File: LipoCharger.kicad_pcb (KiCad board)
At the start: 4 copper layers, 36.2 x 36 mm, 35 parts, among them J1 S2B-XH-A, J2 USB_C_Receptacle_USB2.0_14P, Q1 SI2300A, Q2 SI2300A, Q3 HL 2305A, SW1 SK12D07VG4, U1 TP4056-42-ESOP8, U2 MT3608, U3 FM2113

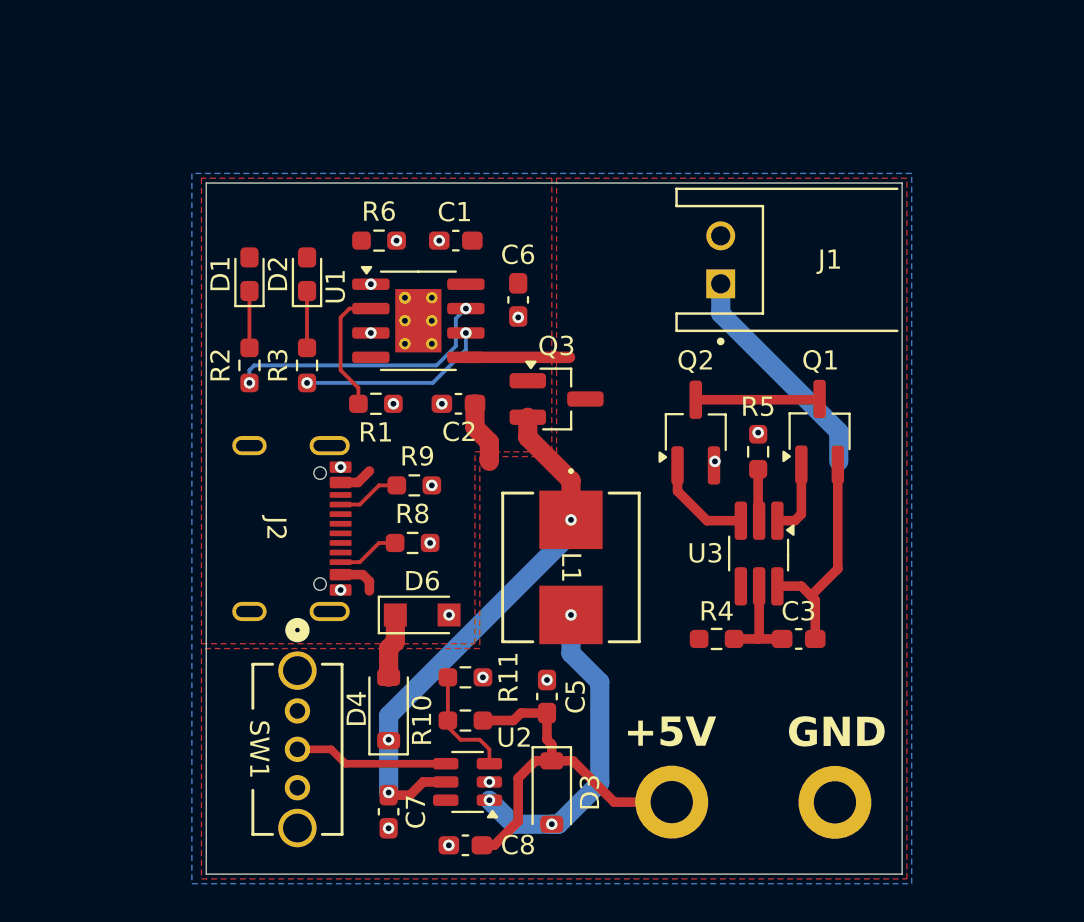
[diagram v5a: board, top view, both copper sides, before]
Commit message: Fixed most of the DRC
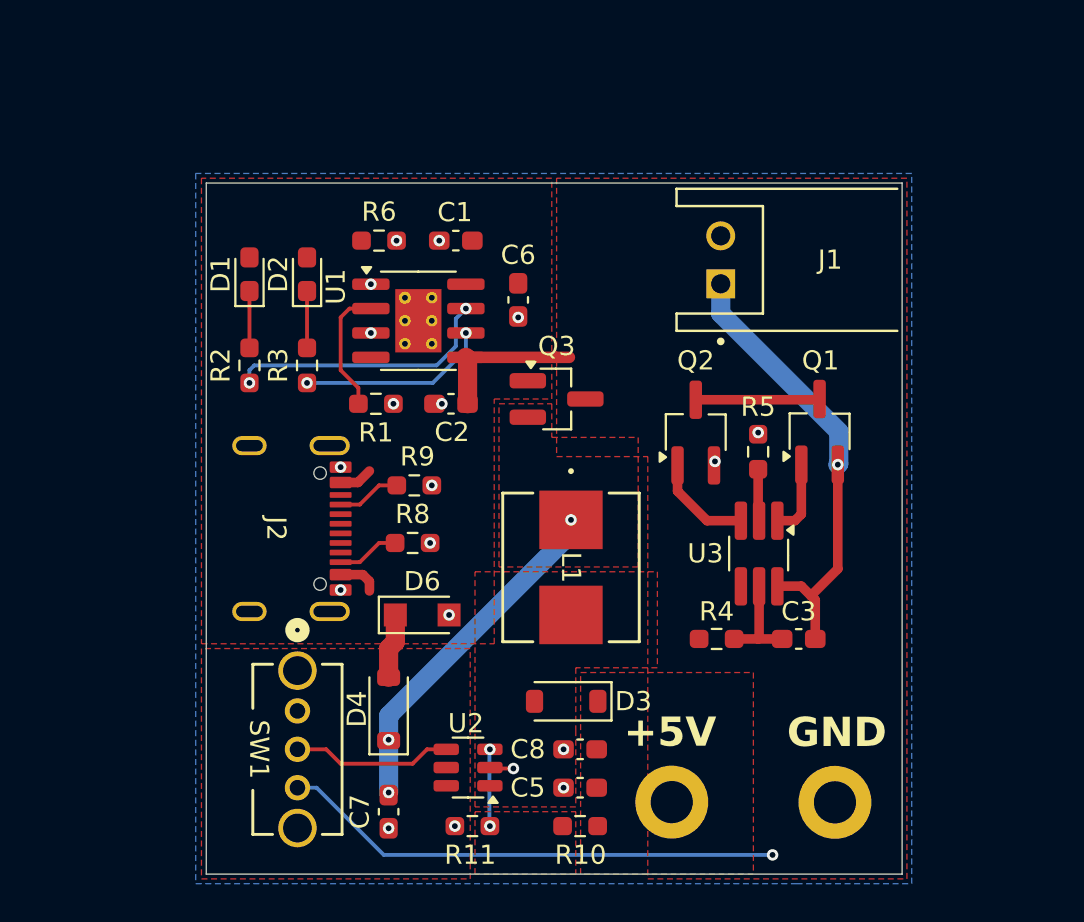
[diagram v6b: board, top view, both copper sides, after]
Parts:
- moved R10 8.12 mm to (49.7, 58.0)
- moved C8 7.79 mm to (49.7, 54.0)
- moved R11 7.76 mm to (44.1, 58.0), turned to 180 degrees
- moved C5 5.05 mm to (49.7, 56.0), turned to 180 degrees
- moved D3 4.81 mm to (49.0, 51.5), turned to 180 degrees
- moved U2 0.75 mm to (43.9, 55.0)
- moved C2 0.39 mm to (43.0, 36.0)
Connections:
- net Net-(D3-A) renamed /SW
- net Net-(D4-K) renamed BOOST_IN
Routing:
- net +BATT: track 8.82 -> 34.2 mm, vias 0 -> 1
- net Net-(D3-K): track 20.0 -> 0.00 mm
- net /SW: track 16.5 -> 0.00 mm, vias 3 -> 0
- net BOOST_IN: track 27.7 -> 18.1 mm
- net Net-(U2-FB): track 5.98 -> 4.02 mm, vias 0 -> 2
- net GND: track 0.31 -> 1.42 mm
- net -BATT: track 23.5 -> 23.7 mm, vias 0 -> 1
- added copper zone on F.Cu, net /SW
- added copper zone on F.Cu, net BOOST_IN
- added copper zone on F.Cu, net Net-(D3-K)
- added copper zone on F.Cu, net Net-(U2-FB)

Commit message: Moved vias outside off of the pads
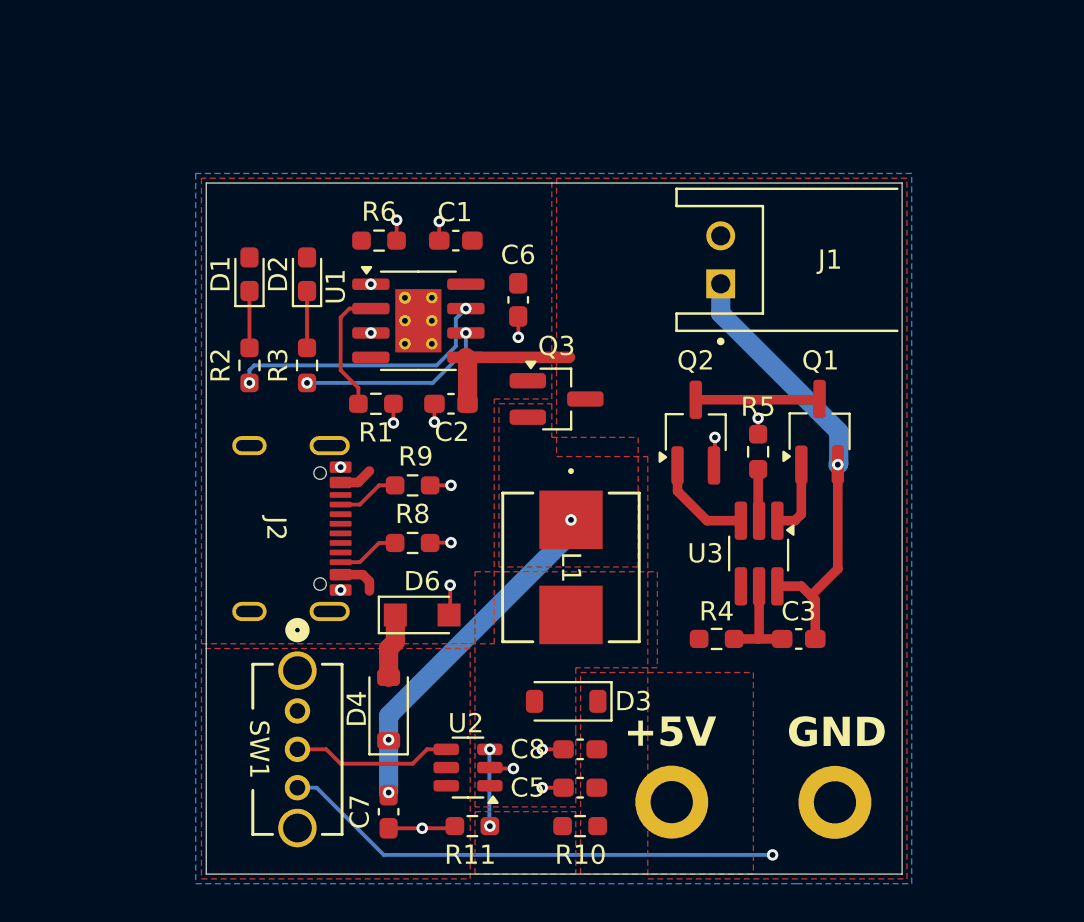
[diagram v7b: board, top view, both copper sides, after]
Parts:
- moved R9 0.09 mm to (41.0, 40.2)
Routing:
- net GND: track 1.42 -> 17.8 mm, vias 19 -> 18
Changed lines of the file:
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@@
 	(footprint "Resistor_SMD:R_0603_1608Metric_Pad0.98x0.95mm_HandSolder"
 		(layer "F.Cu")
-		(at 41.0875 40.25)
+		(at 41 40.25)
 		(descr "Resistor SMD 0603 (1608 Metric), square (rectangular) end terminal, IPC_7351 nominal with elongated pad for handsoldering. (Body size source: IPC-SM-782 page 72, https://www.pcb-3d.com/wordpress/wp-content/uploads/ipc-sm-782a_amendment_1_and_2.pdf), generated with kicad-footprint-generator")
 		(tags "resistor handsolder")
@@
 	)
 	(segment
-		(start 41.9125 43.25)
-		(end 42 43.25)
+		(start 45.075 55)
+		(end 45.025 54.95)
 		(width 0.2)
 		(layer "F.Cu")
@@
 	)
 	(segment
-		(start 45.075 55)
-		(end 45.025 54.95)
+		(start 46.50628 32.536557)
+		(end 46.50628 31.45628)
 		(width 0.2)
 		(layer "F.Cu")
@@
 	)
 	(segment
-		(start 42 40.25)
+		(start 42.957262 45.446719)
+		(end 42.957262 46.942738)
+		(width 0.2)
+		(layer "F.Cu")
+		(net 1)
+	)
+	(segment
+		(start 42.3875 26.5)
+		(end 42.3875 27.5)
+		(width 0.2)
+		(layer "F.Cu")
+		(net 1)
+	)
+	(segment
+		(start 47.75 56)
+		(end 48.8625 56)
+		(width 0.2)
+		(layer "F.Cu")
+		(net 1)
+	)
+	(segment
+		(start 40 37)
+		(end 40 36)
+		(width 0.2)
+		(layer "F.Cu")
+		(net 1)
+	)
+	(segment
+		(start 47.75 54)
+		(end 48.8625 54)
+		(width 0.2)
+		(layer "F.Cu")
+		(net 1)
+	)
+	(segment
+		(start 46.50628 31.45628)
+		(end 46.5 31.45)
+		(width 0.2)
+		(layer "F.Cu")
+		(net 1)
+	)
+	(segment
+		(start 40.167955 27.494545)
+		(end 40.1625 27.5)
+		(width 0.2)
+		(layer "F.Cu")
+		(net 1)
+	)
+	(segment
+		(start 43 40.25)
 		(end 42.0875 40.25)
 		(width 0.2)
@@
 		(net 1)
 	)
+	(segment
+		(start 40.167955 26.432615)
+		(end 40.167955 27.494545)
+		(width 0.2)
+		(layer "F.Cu")
+		(net 1)
+	)
+	(segment
+		(start 39.75 58.1125)
+		(end 41.5 58.1125)
+		(width 0.2)
+		(layer "F.Cu")
+		(net 1)
+	)
+	(segment
+		(start 42.136947 36.000553)
+		(end 42.1375 36)
+		(width 0.2)
+		(layer "F.Cu")
+		(net 1)
+	)
+	(segment
+		(start 41.5 58.1125)
+		(end 43.0875 58.1125)
+		(width 0.2)
+		(layer "F.Cu")
+		(net 1)
+	)
+	(segment
+		(start 42.136947 36.95589)
+		(end 42.136947 36.000553)
+		(width 0.2)
+		(layer "F.Cu")
+		(net 1)
+	)
+	(segment
+		(start 56.75 37.75)
+		(end 56.75 39.16)
+		(width 0.2)
+		(layer "F.Cu")
+		(net 1)
+	)
+	(segment
+		(start 43 43.23278)
+		(end 42.099949 43.23278)
+		(width 0.2)
+		(layer "F.Cu")
+		(net 1)
+	)
+	(segment
+		(start 43.0875 58.1125)
+		(end 43.2 58)
+		(width 0.2)
+		(layer "F.Cu")
+		(net 1)
+	)
+	(segment
+		(start 42.957262 46.942738)
+		(end 42.9 47)
+		(width 0.2)
+		(layer "F.Cu")
+		(net 1)
+	)
+	(segment
+		(start 59 37.5875)
+		(end 59 36.75)
+		(width 0.2)
+		(layer "F.Cu")
+		(net 1)
+	)
+	(segment
+		(start 56.75 39.16)
+		(end 56.7 39.21)
+		(width 0.2)
+		(layer "F.Cu")
+		(net 1)
+	)
 	(via
-		(at 39.75 58.1125)
+		(at 41.5 58.1125)
 		(size 0.6)
 		(drill 0.3)
@@
 	)
 	(via
-		(at 46.5 31.5)
+		(at 46.50628 32.536557)
 		(size 0.6)
 		(drill 0.3)
@@
 	)
 	(via
-		(at 56.75 39)
+		(at 56.75 37.75)
 		(size 0.6)
 		(drill 0.3)
@@
 	)
 	(via
-		(at 40.1625 27.5)
+		(at 40.167955 26.432615)
 		(size 0.6)
 		(drill 0.3)
@@
 	)
 	(via
-		(at 41.9125 43.25)
+		(at 43 43.23278)
 		(size 0.6)
 		(drill 0.3)
@@
 	)
 	(via
-		(at 48.8625 56)
+		(at 47.75 56)
 		(size 0.6)
 		(drill 0.3)
@@
 	)
 	(via
-		(at 42 40.25)
+		(at 43 40.25)
 		(size 0.6)
 		(drill 0.3)
@@
 	)
 	(via
-		(at 42.525 36)
+		(at 42.136947 36.95589)
 		(size 0.6)
 		(drill 0.3)
@@
 	)
 	(via
-		(at 48.8625 54)
+		(at 47.75 54)
 		(size 0.6)
 		(drill 0.3)
@@
 	)
 	(via
-		(at 59 37.5)
+		(at 59 36.75)
 		(size 0.6)
 		(drill 0.3)
@@
 	)
 	(via
-		(at 40 36)
+		(at 40 37)
 		(size 0.6)
 		(drill 0.3)
@@
 	)
 	(via
-		(at 42.3875 27.5)
+		(at 42.3875 26.5)
 		(size 0.6)
 		(drill 0.3)
@@
 	)
 	(via
-		(at 42.9 47)
+		(at 42.957262 45.446719)
 		(size 0.6)
 		(drill 0.3)
@@
 	)
 	(via
-		(at 43.2 58)
-		(size 0.6)
-		(drill 0.3)
-		(layers "F.Cu" "B.Cu")
-		(net 1)
-	)
-	(via
 		(at 43.775 32.31)
 		(size 0.6)
@@
 	)
 	(segment
-		(start 38.25 41.25)
-		(end 39.25 40.25)
+		(start 39.25 40.25)
+		(end 40.0875 40.25)
 		(width 0.2)
 		(layer "F.Cu")
@@
 	)
 	(segment
-		(start 39.25 40.25)
-		(end 40.175 40.25)
+		(start 38.25 41.25)
+		(end 39.25 40.25)
 		(width 0.2)
 		(layer "F.Cu")

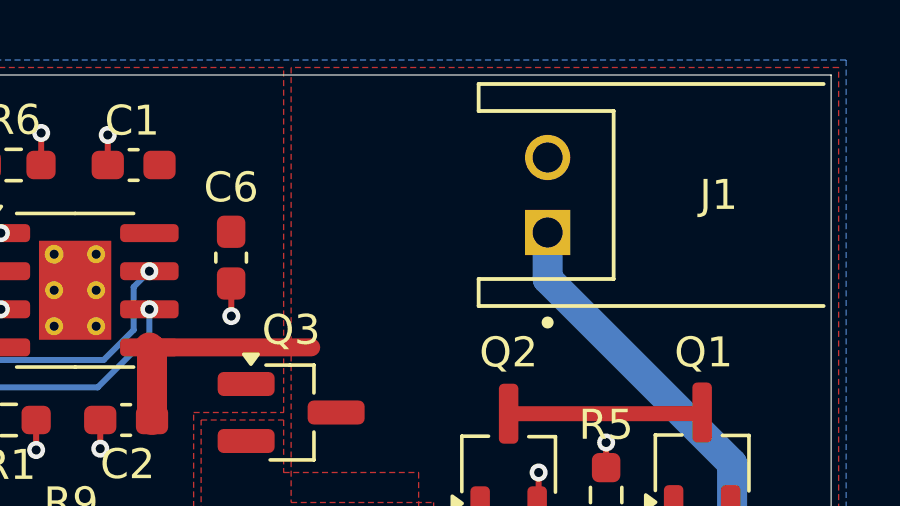
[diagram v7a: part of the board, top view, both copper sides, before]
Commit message: Updated LCSC Part Numbers
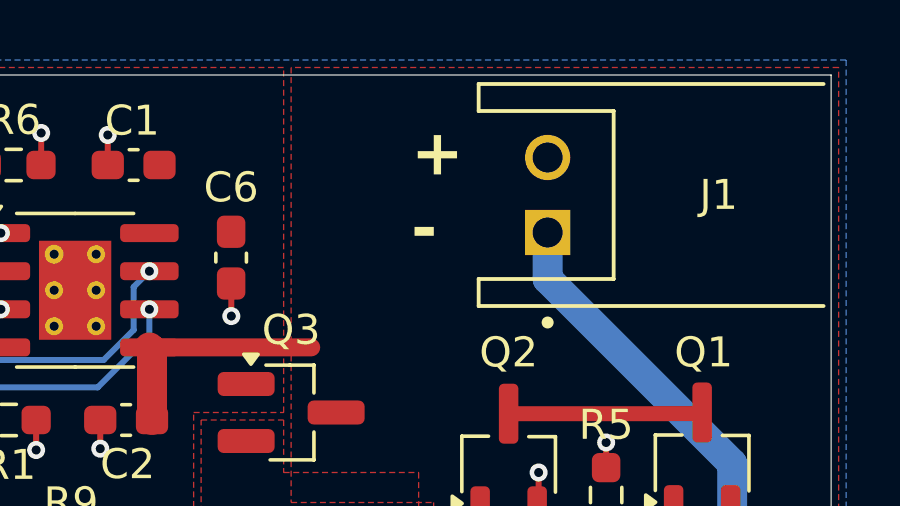
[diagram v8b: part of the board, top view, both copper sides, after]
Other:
- board text added: "+"
- board text added: "-"
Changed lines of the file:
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@@
 			)
 		)
+		(property "LCSC Part #" "C347480"
+			(at 0 0 90)
+			(unlocked yes)
+			(layer "F.Fab")
+			(hide yes)
+			(effects
+				(font
+					(size 1 1)
+					(thickness 0.15)
+				)
+			)
+		)
 		(sheetname "/")
 		(sheetfile "LipoCharger.kicad_sch")
@@
 			)
 		)
+		(property "LCSC Part #" "C347480"
+			(at 0 0 90)
+			(unlocked yes)
+			(layer "F.Fab")
+			(hide yes)
+			(effects
+				(font
+					(size 1 1)
+					(thickness 0.15)
+				)
+			)
+		)
 		(sheetname "/")
 		(sheetfile "LipoCharger.kicad_sch")
@@
 			)
 		)
-		(property "LCSC Part #" "C59461"
+		(property "LCSC Part #" "C6119863"
 			(at 0 0 180)
 			(unlocked yes)
@@
 			)
 		)
-		(property "LCSC Part #" "C19702"
+		(property "LCSC Part #" "C6119863"
 			(at 0 0 180)
 			(unlocked yes)
@@
 			)
 		)
-		(property "LCSC Part #" "C19702"
+		(property "LCSC Part #" "C6119863"
 			(at 0 0 180)
 			(unlocked yes)
@@
 			)
 		)
+		(property "LCSC Part #" "C98220"
+			(at 0 0 180)
+			(unlocked yes)
+			(layer "F.Fab")
+			(hide yes)
+			(effects
+				(font
+					(size 1 1)
+					(thickness 0.15)
+				)
+			)
+		)
 		(property ki_fp_filters "R_*")
 		(sheetname "/")
@@
 			)
 		)
-		(property "LCSC Part #" "C19702"
+		(property "LCSC Part #" "C5137636"
 			(at 0 0 270)
 			(unlocked yes)
@@
 			)
 		)
-		(property "LCSC Part #" "C59461"
+		(property "LCSC Part #" "C6119863"
 			(at 0 0 180)
 			(unlocked yes)
@@
 			)
 		)
-		(property "LCSC Part #" "C14663"
+		(property "LCSC Part #" "C5137636"
 			(at 0 0 0)
 			(unlocked yes)
@@
 			)
 		)
-		(property "LCSC Part #" "C98220"
+		(property "LCSC Part #" "C137801"
 			(at 0 0 180)
 			(unlocked yes)
@@
 		(layer "Edge.Cuts")
 	)
+	(gr_text "-"
+		(at 52.5 30.5 0)
+		(layer "F.SilkS")
+		(effects
+			(font
+				(size 1.524 1.524)
+				(thickness 0.3048)
+				(bold yes)
+			)
+			(justify left bottom)
+		)
+	)
+	(gr_text "+"
+		(at 52.5 28 0)
+		(layer "F.SilkS")
+		(effects
+			(font
+				(size 1.524 1.524)
+				(thickness 0.3048)
+				(bold yes)
+			)
+			(justify left bottom)
+		)
+	)
 	(gr_text "GND"
